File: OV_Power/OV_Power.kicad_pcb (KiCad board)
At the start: 2 copper layers, 100 x 100 mm, 79 parts, among them CN1 CONN_HEADER_R_A_2POS_2.5MM, J1 OpenVent_Barrel_Connector, J2 Conn_HDR_2x10_latching, Q1 SSM3K341R, Q2 2N7002BK, U1 LT3796, U2 LT1936, U3 LMC6772AIMX, U4 VNH5019ATR-E, U5 CSD88537ND, U6 LTC4365xTS8, U7 LTC4416, U8 AOSD21307, U9 AOSD21307

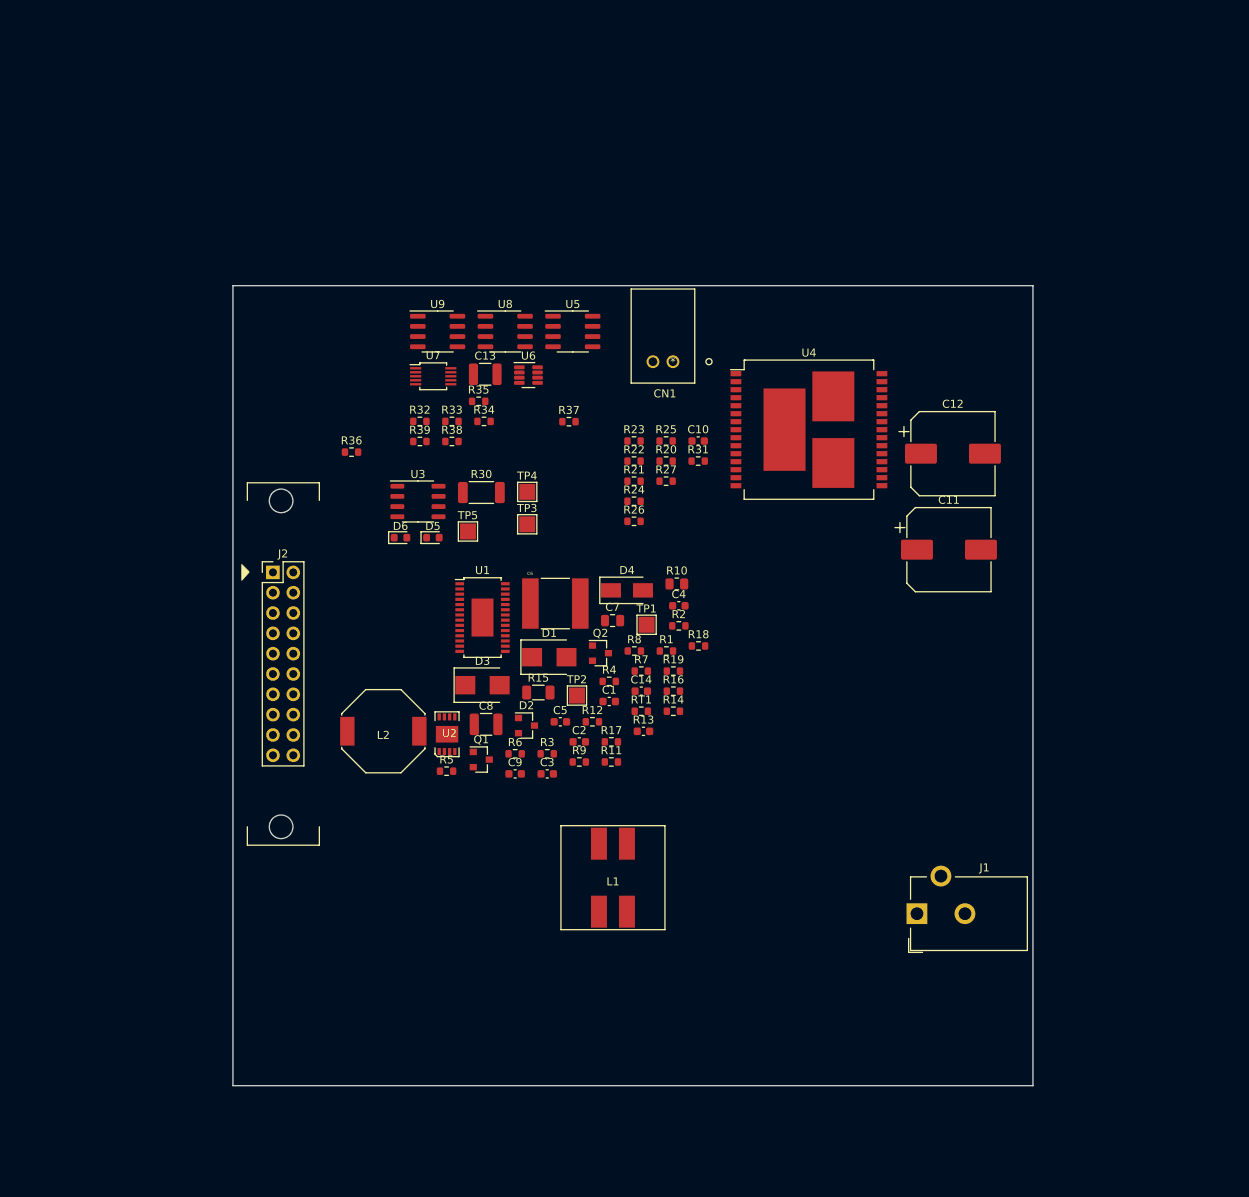
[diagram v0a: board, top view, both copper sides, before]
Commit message: New board outline and power connector added.  Still need definition of connector for microswitches and schematic.
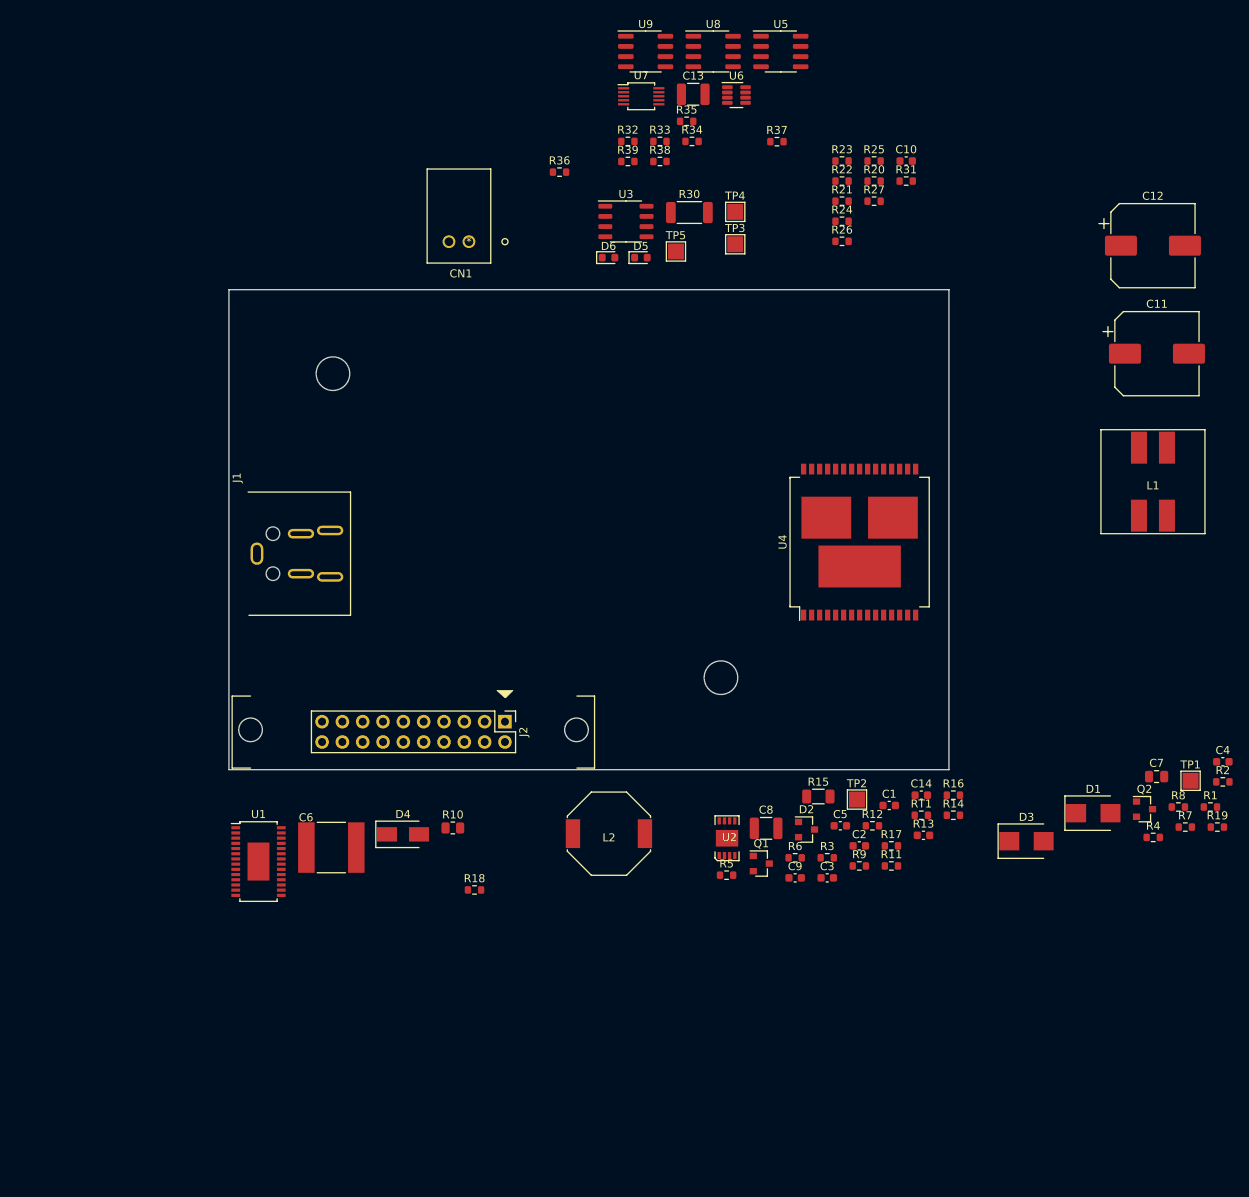
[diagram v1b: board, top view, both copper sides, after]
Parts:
- added REF**: MountingHole_4.2x9mm, OpenVent:MountingHole_4.2x9mm, F.Cu at (91.5, 78.5)
- added REF**: MountingHole_4.2x9mm, OpenVent:MountingHole_4.2x9mm, F.Cu at (43.0, 40.5)
- J1: value OpenVent_Barrel_Connector -> Kycon_kpjx-4s; footprint Connector_BarrelJack:BarrelJack_CUI_PJ-102AH_Horizontal -> OpenVent:Kycon_KPJX-4S
- moved J1 94.0 mm to (33.5, 63.0)
- moved L1 83.7 mm to (145.5, 54.0)
- moved C4 70.7 mm to (154.2, 89.0)
- moved C7 70.7 mm to (146.0, 90.9)
- moved D1 70.7 mm to (138.0, 95.4)
- moved R2 70.7 mm to (154.2, 91.5)
- moved R7 70.7 mm to (149.5, 97.2)
- moved R8 70.7 mm to (148.7, 94.7)
- moved TP1 70.7 mm to (150.2, 91.4)
- moved D3 70.7 mm to (129.7, 98.9)
- moved R1 70.7 mm to (152.7, 94.7)
- moved R19 70.7 mm to (153.6, 97.2)
- moved R4 70.7 mm to (145.5, 98.5)
- moved Q2 70.7 mm to (144.4, 94.9)
- moved C10 43.6 mm to (114.7, 13.9)
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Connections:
- J1 pad 3: Net-(J1-Pad3) -> GND
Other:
- board size 100 x 100 mm -> 90 x 60 mm

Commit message: Getting on with the placement of the power board, functional blocks are all grouped together, just need to fit them all in now.
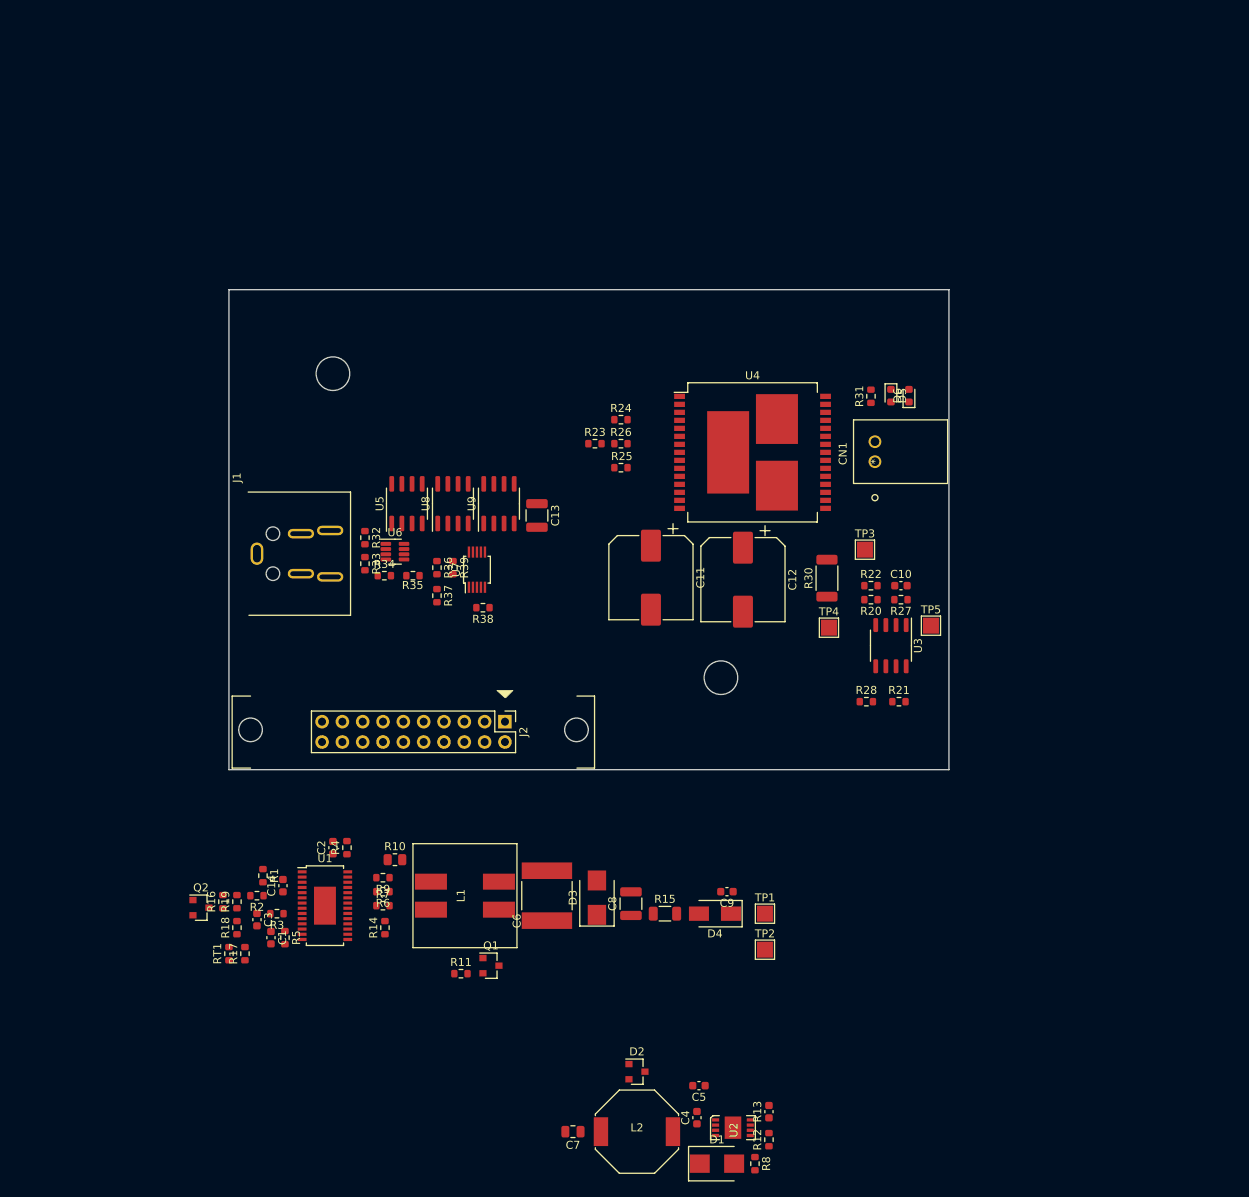
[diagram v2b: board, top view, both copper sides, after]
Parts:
- added R28: 10k_0603_Chip_Resistor,_1%,_0.1W, Resistor_SMD:R_0603_1608Metric, F.Cu at (109.7, 81.5)
- R21: value 215k_0603_Chip_Resistor,_1%,_0.1W -> 10k_0603_Chip_Resistor,_1%,_0.1W
- moved R19 122.9 mm to (31.0, 106.5), turned to 90 degrees
- moved R2 121.6 mm to (33.5, 105.8), turned to 180 degrees
- moved R1 118.7 mm to (34.2, 103.2), turned to 270 degrees
- moved Q2 118.6 mm to (26.5, 107.2)
- moved R4 100.8 mm to (44.8, 99.8), turned to 90 degrees
- moved R7 100.8 mm to (49.2, 107.0)
- moved L1 100.4 mm to (59.5, 105.8), turned to 270 degrees
- moved R16 92.3 mm to (29.2, 106.5), turned to 90 degrees
- moved RT1 88.3 mm to (30.0, 113.0), turned to 90 degrees
- moved C7 85.4 mm to (73.0, 135.2), turned to 180 degrees
- moved R17 81.9 mm to (32.0, 113.0), turned to 90 degrees
- moved C14 80.6 mm to (36.8, 104.5), turned to 90 degrees
- moved C4 79.4 mm to (88.5, 133.5), turned to 90 degrees
- moved C1 79.0 mm to (35.2, 111.0), turned to 270 degrees
- moved U5 73.3 mm to (52.2, 56.8), turned to 90 degrees
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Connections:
- net VBUS renamed VBATT
- net VIN renamed VIN_12V
- C11 pad 1: +5V -> V_MAIN
- C12 pad 1: +5V -> V_MAIN
- C13 pad 1: +5V -> V_MAIN
- C4 pad 1: +5V -> V_MAIN
- J2 pad 2: +5V -> V_MAIN
- R21 pad 1: Net-(R20-Pad1) -> Net-(R21-Pad1)
- R21 pad 2: /Motor Driver/BIAS -> +3V3
- U2 pad 2: +5V -> V_MAIN
- U3 pad 5: GND -> Net-(R28-Pad2)
- U3 pad 6: +3V3 -> Net-(R21-Pad1)
- U4 pad 12: +5V -> V_MAIN
- U4 pad 13: +5V -> V_MAIN
- U4 pad 23: +5V -> V_MAIN
- U4 pad 3: +5V -> V_MAIN
- U4 pad 31: +5V -> V_MAIN
- U7 pad 8: +5V -> V_MAIN
- U8 pad 3: +5V -> V_MAIN
- U9 pad 1: +5V -> V_MAIN

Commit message: Continuing to refine both the schemo and placement for the power supply board.  I think we have all the connectors we need now...
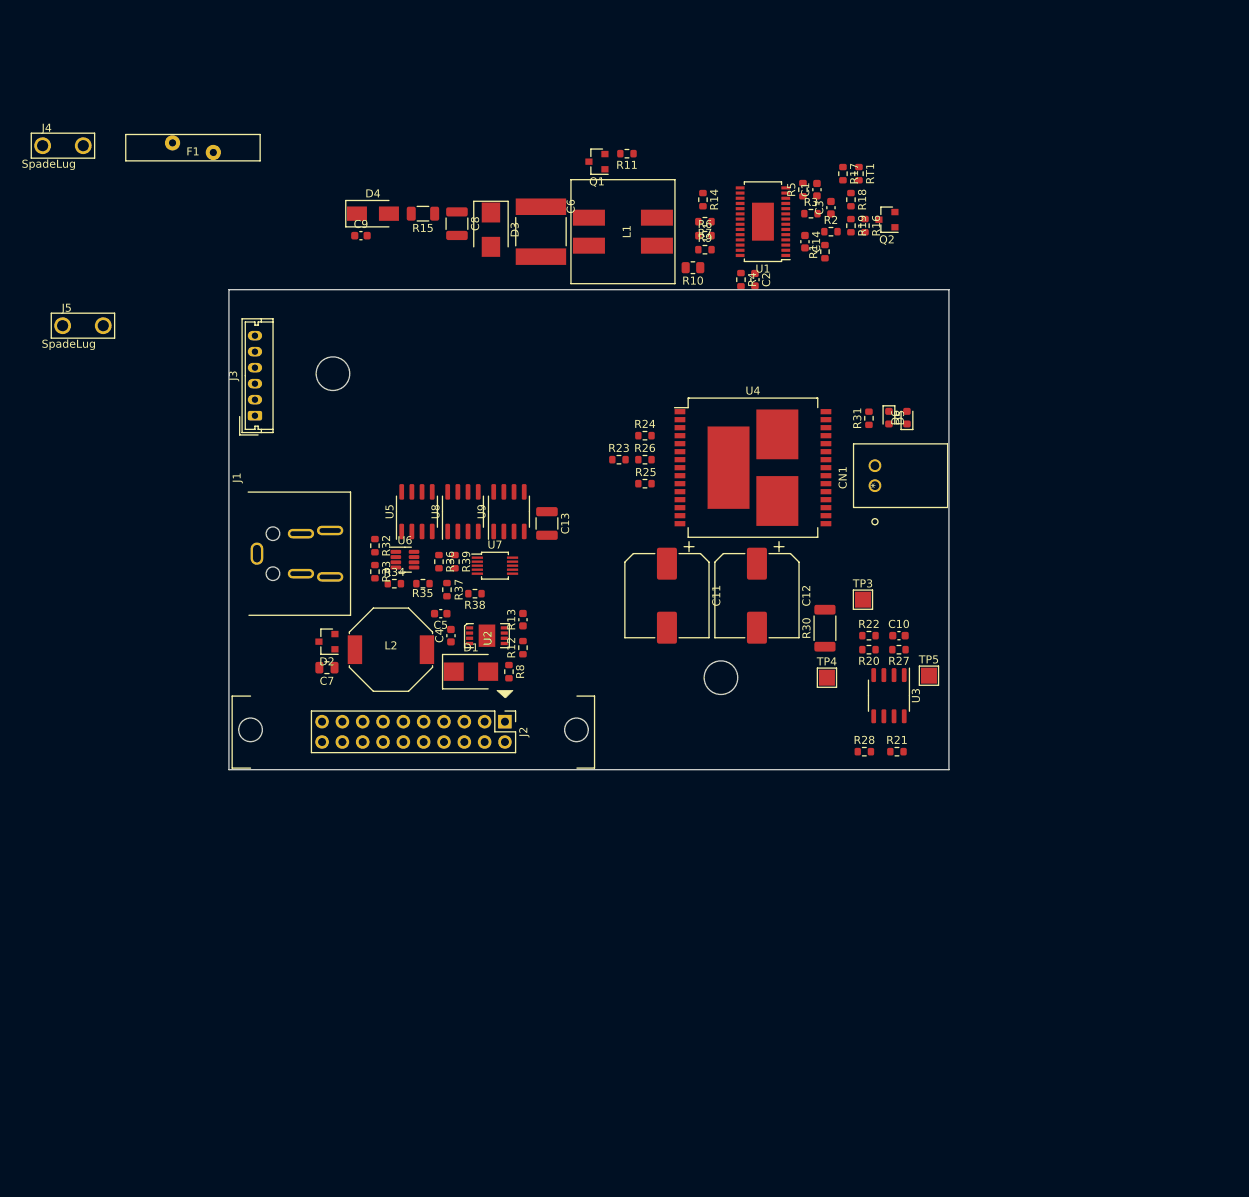
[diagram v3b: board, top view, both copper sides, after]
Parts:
- removed TP1, TP2: Test_Point_PTH, TestPoint:TestPoint_Pad_2.0x2.0mm
- added F1: Polyfuse_10A, OpenVent:LF_16R1000G, F.Cu at (25.5, 12.2)
- added J3: 532530670, Connector_Molex:Molex_Micro-Latch_53253-0670_1x06_P2.00mm_Vertical, F.Cu at (33.2, 45.8)
- added J4: SpadeLug, F_Connectors:TE_1217861-1, F.Cu at (9.25, 12.0)
- added J5: SpadeLug, F_Connectors:TE_1217861-1, F.Cu at (11.8, 34.5)
- moved RT1 125.3 mm to (108.8, 15.5), turned to 270 degrees
- moved R17 122.9 mm to (106.8, 15.5), turned to 270 degrees
- moved Q2 121.4 mm to (112.2, 21.2), turned to 180 degrees
- moved R18 119.0 mm to (107.8, 18.8), turned to 270 degrees
- moved R16 116.5 mm to (109.5, 22.0), turned to 270 degrees
- moved C1 115.8 mm to (103.5, 17.5), turned to 90 degrees
- moved C3 114.3 mm to (105.2, 19.8), turned to 90 degrees
- moved R19 114.2 mm to (107.8, 22.0), turned to 270 degrees
- moved R5 113.7 mm to (101.8, 17.5), turned to 90 degrees
- moved R3 110.1 mm to (102.8, 20.5), turned to 0 degrees
- moved R2 109.7 mm to (105.2, 22.8), turned to 0 degrees
- moved R1 105.0 mm to (104.5, 25.2), turned to 90 degrees
- moved R11 104.6 mm to (79.8, 13.0), turned to 180 degrees
- moved C14 103.6 mm to (102.0, 24.0), turned to 270 degrees
- moved U1 101.5 mm to (96.8, 21.5), turned to 180 degrees
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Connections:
- J2 pad 10: GND -> Net-(J2-Pad10)

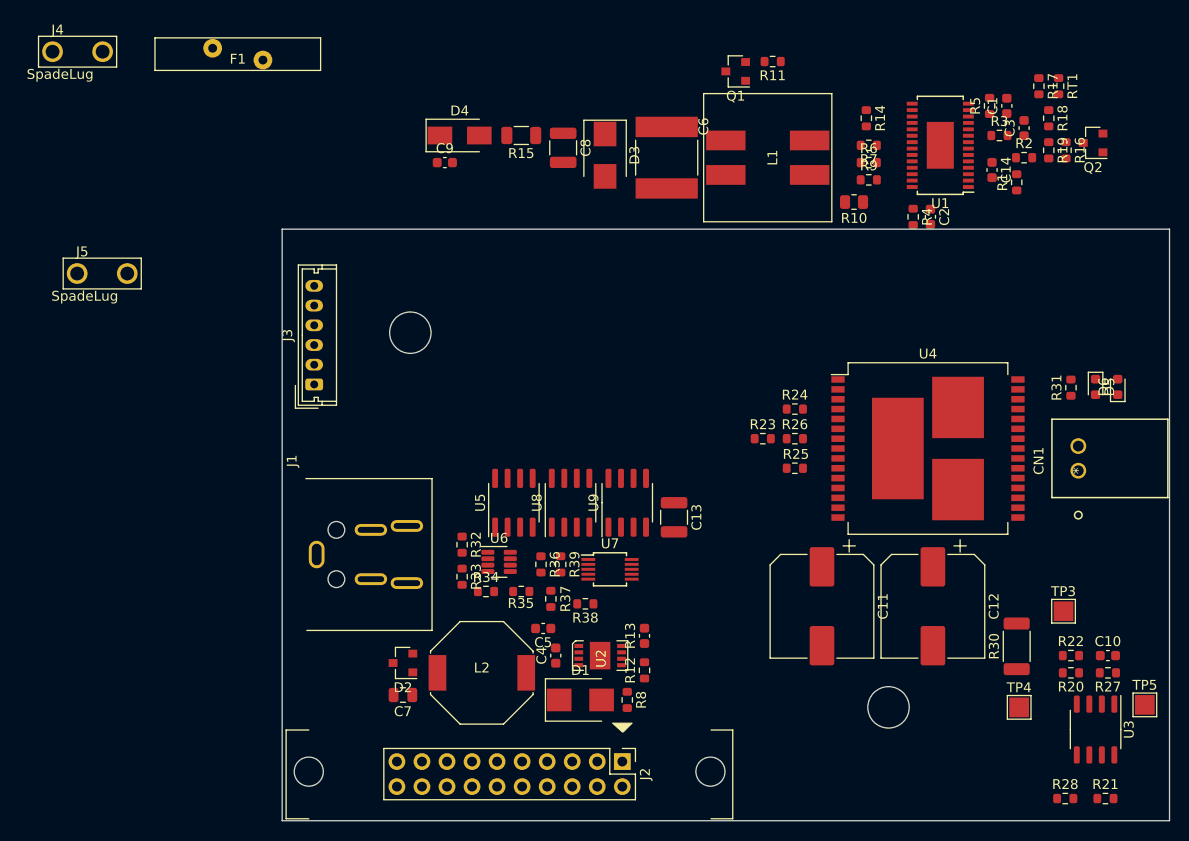
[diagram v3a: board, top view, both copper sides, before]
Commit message: Finished off a tentative placement for the power board.
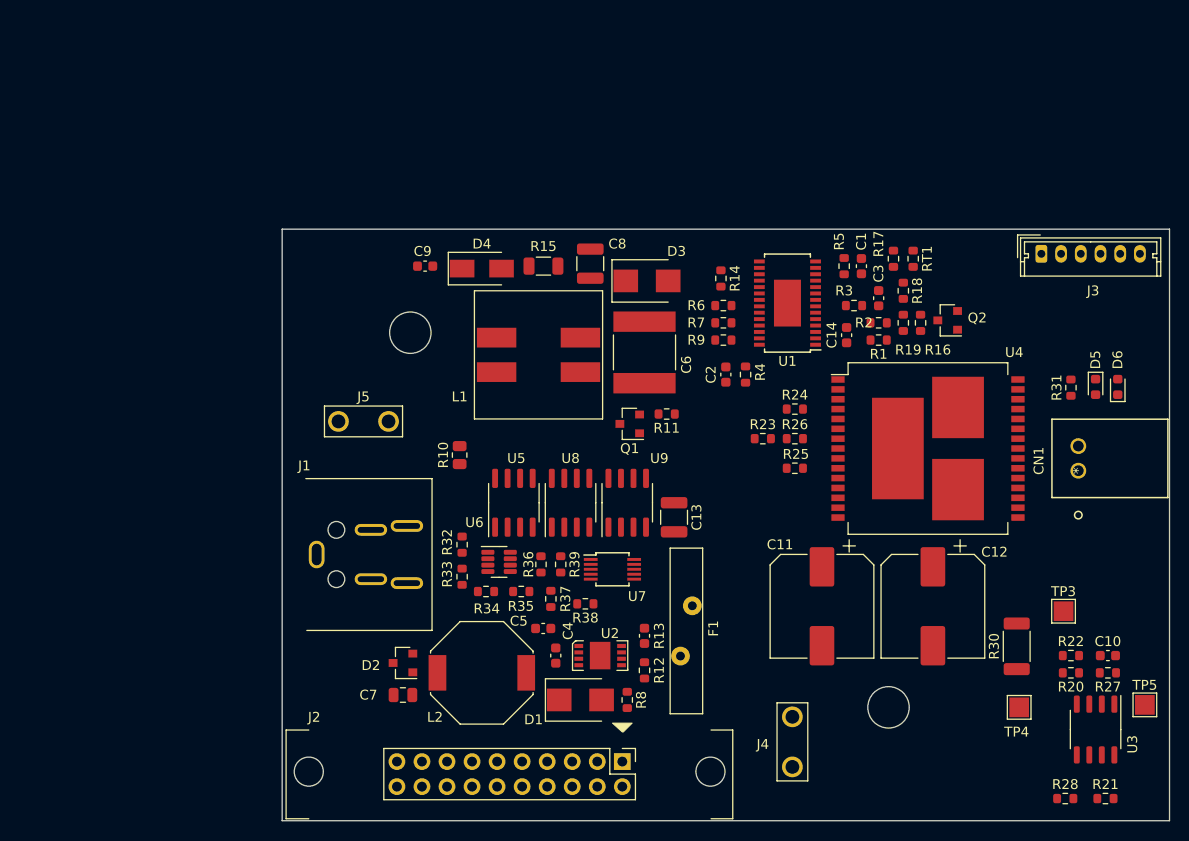
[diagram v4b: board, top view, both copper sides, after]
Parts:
- moved J4 100.8 mm to (81.8, 82.0), turned to 90 degrees
- moved J3 74.9 mm to (107.0, 32.5), turned to 0 degrees
- moved F1 74.1 mm to (71.0, 70.8), turned to 90 degrees
- moved R10 47.5 mm to (48.0, 52.9), turned to 90 degrees
- moved Q1 37.3 mm to (65.2, 49.8)
- moved R11 37.3 mm to (69.0, 48.8)
- moved L1 30.7 mm to (56.0, 42.8), turned to 270 degrees
- moved J5 30.5 mm to (38.2, 49.5)
- moved C2 26.2 mm to (75.0, 44.8)
- moved R4 23.3 mm to (77.0, 44.8)
- moved Q2 23.3 mm to (97.5, 39.2)
- moved R16 22.9 mm to (94.8, 39.5)
- moved R17 22.9 mm to (92.0, 33.0)
- moved R18 22.9 mm to (93.0, 36.2)
- moved R19 22.9 mm to (93.0, 39.5)
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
